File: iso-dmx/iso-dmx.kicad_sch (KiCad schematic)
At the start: 8 parts, among them J1 Conn_01x06, J2 Conn_01x06, U1 ISO1432BDW

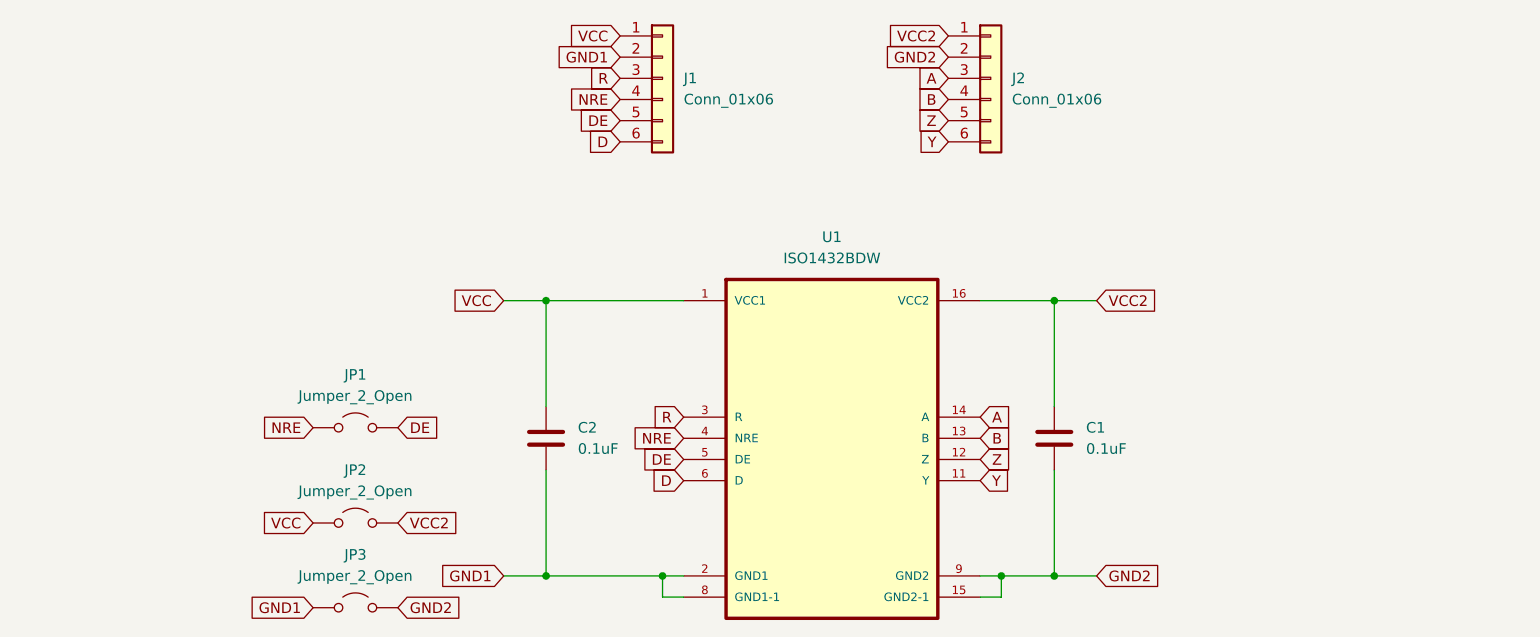
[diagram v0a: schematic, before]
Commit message: Added isolated voltage regulator to RS485 board
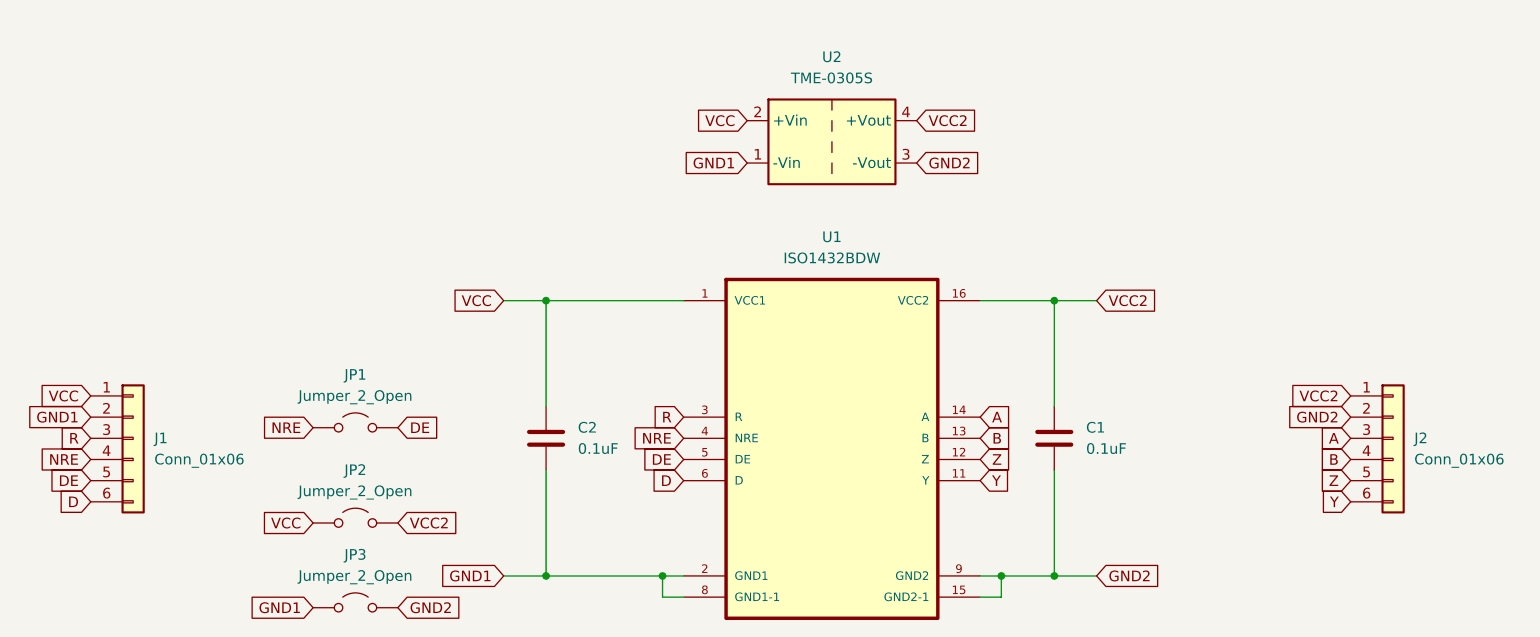
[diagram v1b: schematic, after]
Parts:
- added U2: TME-0305S, Converter_DCDC:Converter_DCDC_TRACO_TME_03xxS_05xxS_12xxS_Single_THT, symbol Converter_DCDC:TME-0305S
- C1, C2: footprint Capacitor_SMD:C_0603_1608Metric_Pad1.08x0.95mm_HandSolder -> Capacitor_SMD:C_1206_3216Metric_Pad1.33x1.80mm_HandSolder
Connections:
- net GND1: now also U2.1 (-Vin)
- net GND2: now also U2.3 (-Vout)
- net VCC: now also U2.2 (+Vin)
- net VCC2: now also U2.4 (+Vout)
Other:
- moved on the sheet: J1, J2
